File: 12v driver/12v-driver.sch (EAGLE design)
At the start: 42 parts, among them IC1 74AC14N, IC2 74AC14N, Q1 2N3906, Q2 2N3906, T1 2N3904, T2 2N3904, T3 2N3904, T4 2N3904, T5 2N3904, T6 2N3904

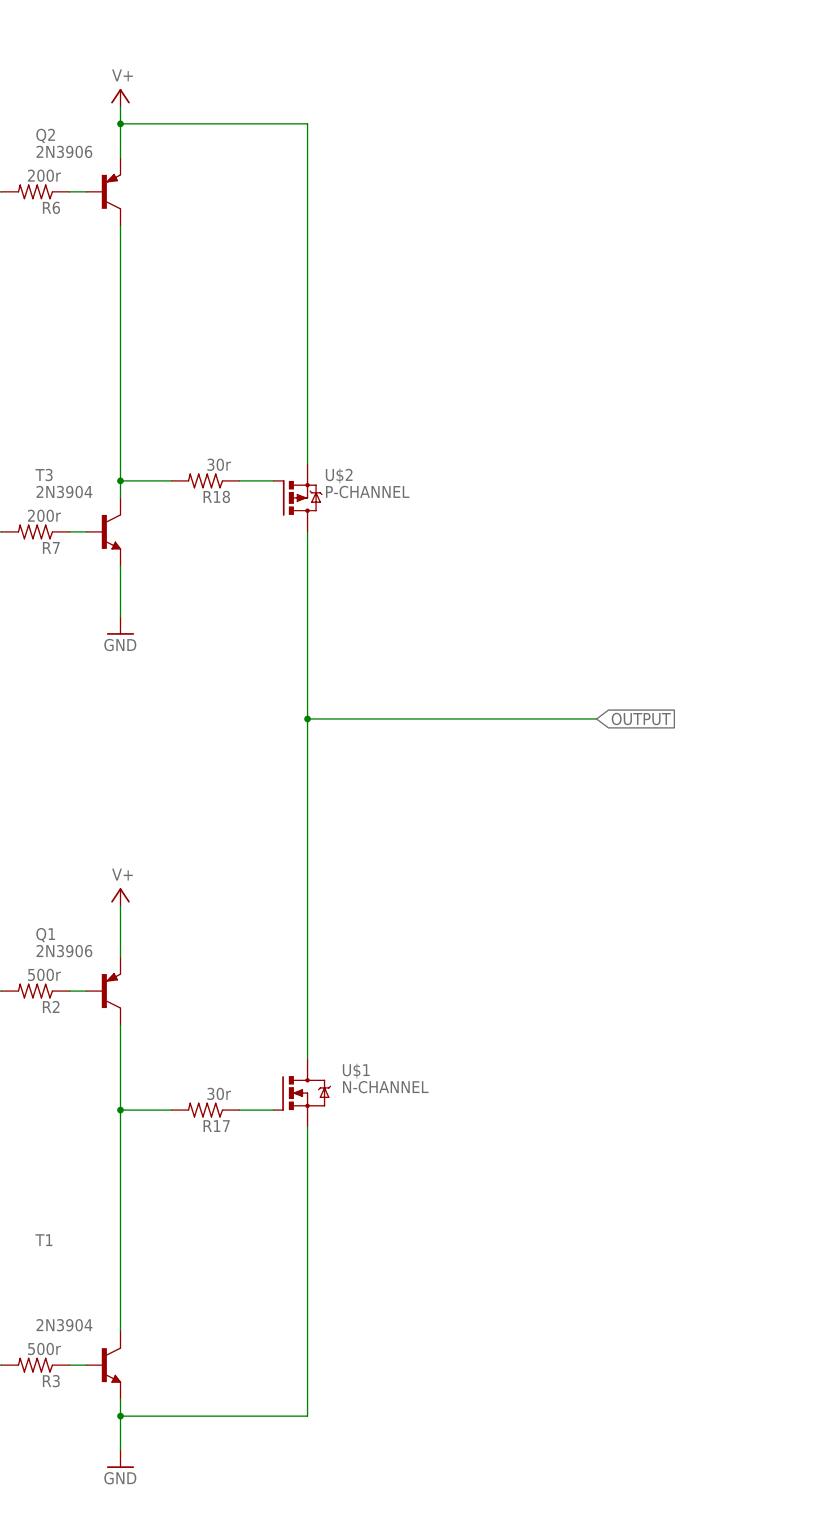
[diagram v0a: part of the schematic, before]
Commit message: added inverter to driver NPNs
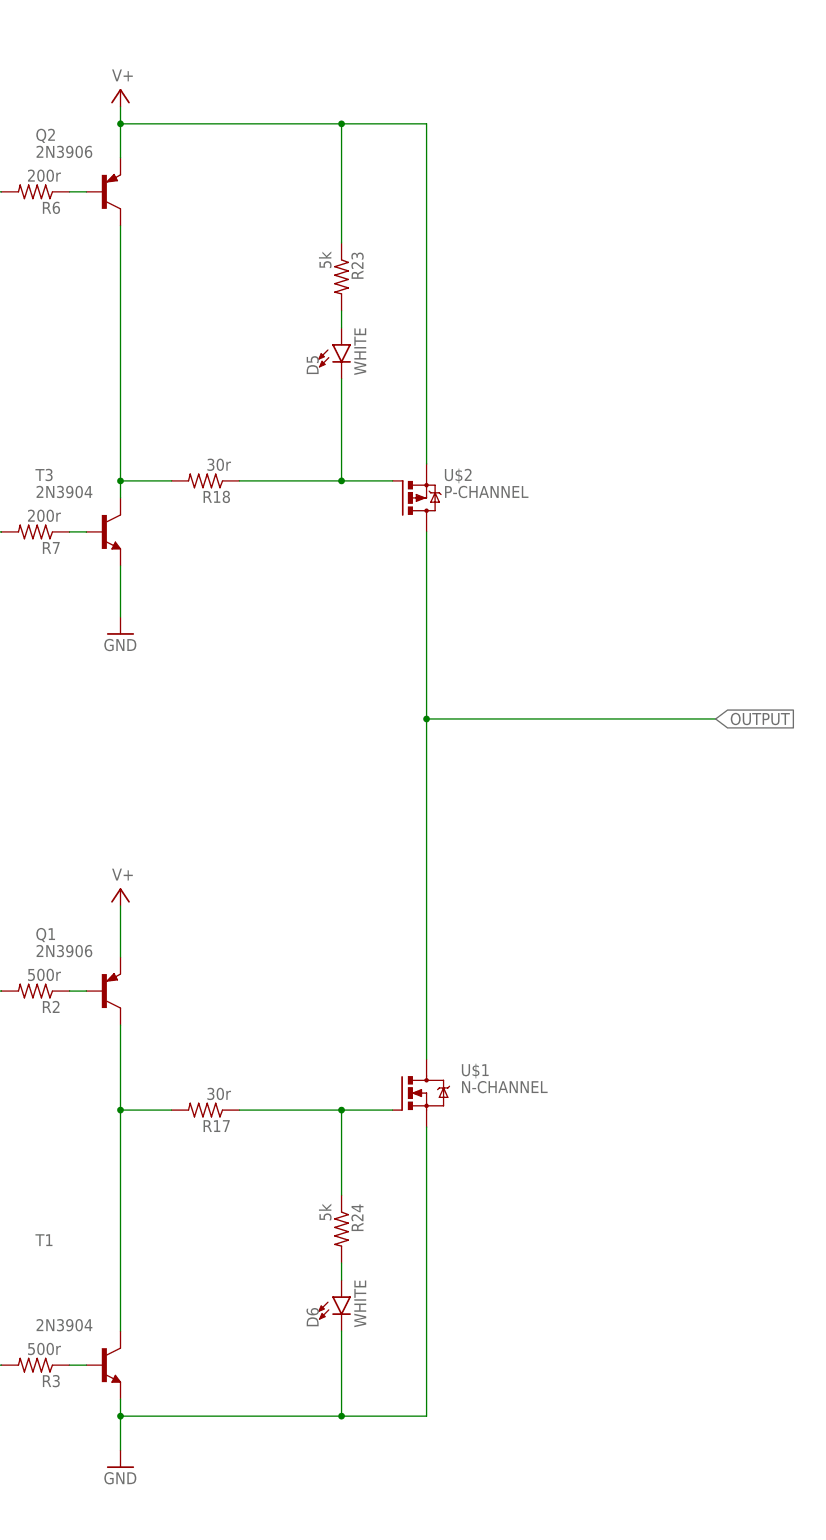
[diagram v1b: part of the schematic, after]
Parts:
- added D5, D6: WHITE, SparkFun-LED:LED-WHITE1206
- added R23, R24: 5k, rcl:R-US_R0603
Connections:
- new net N$29: D5.A, R23.2
- new net N$30: D6.A, R24.2
- net GND: now also D6.C
- net N$2: now also R24.1
- net N$8: now also D5.C
- net V+: now also R23.1
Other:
- moved on the sheet: U$1, U$2

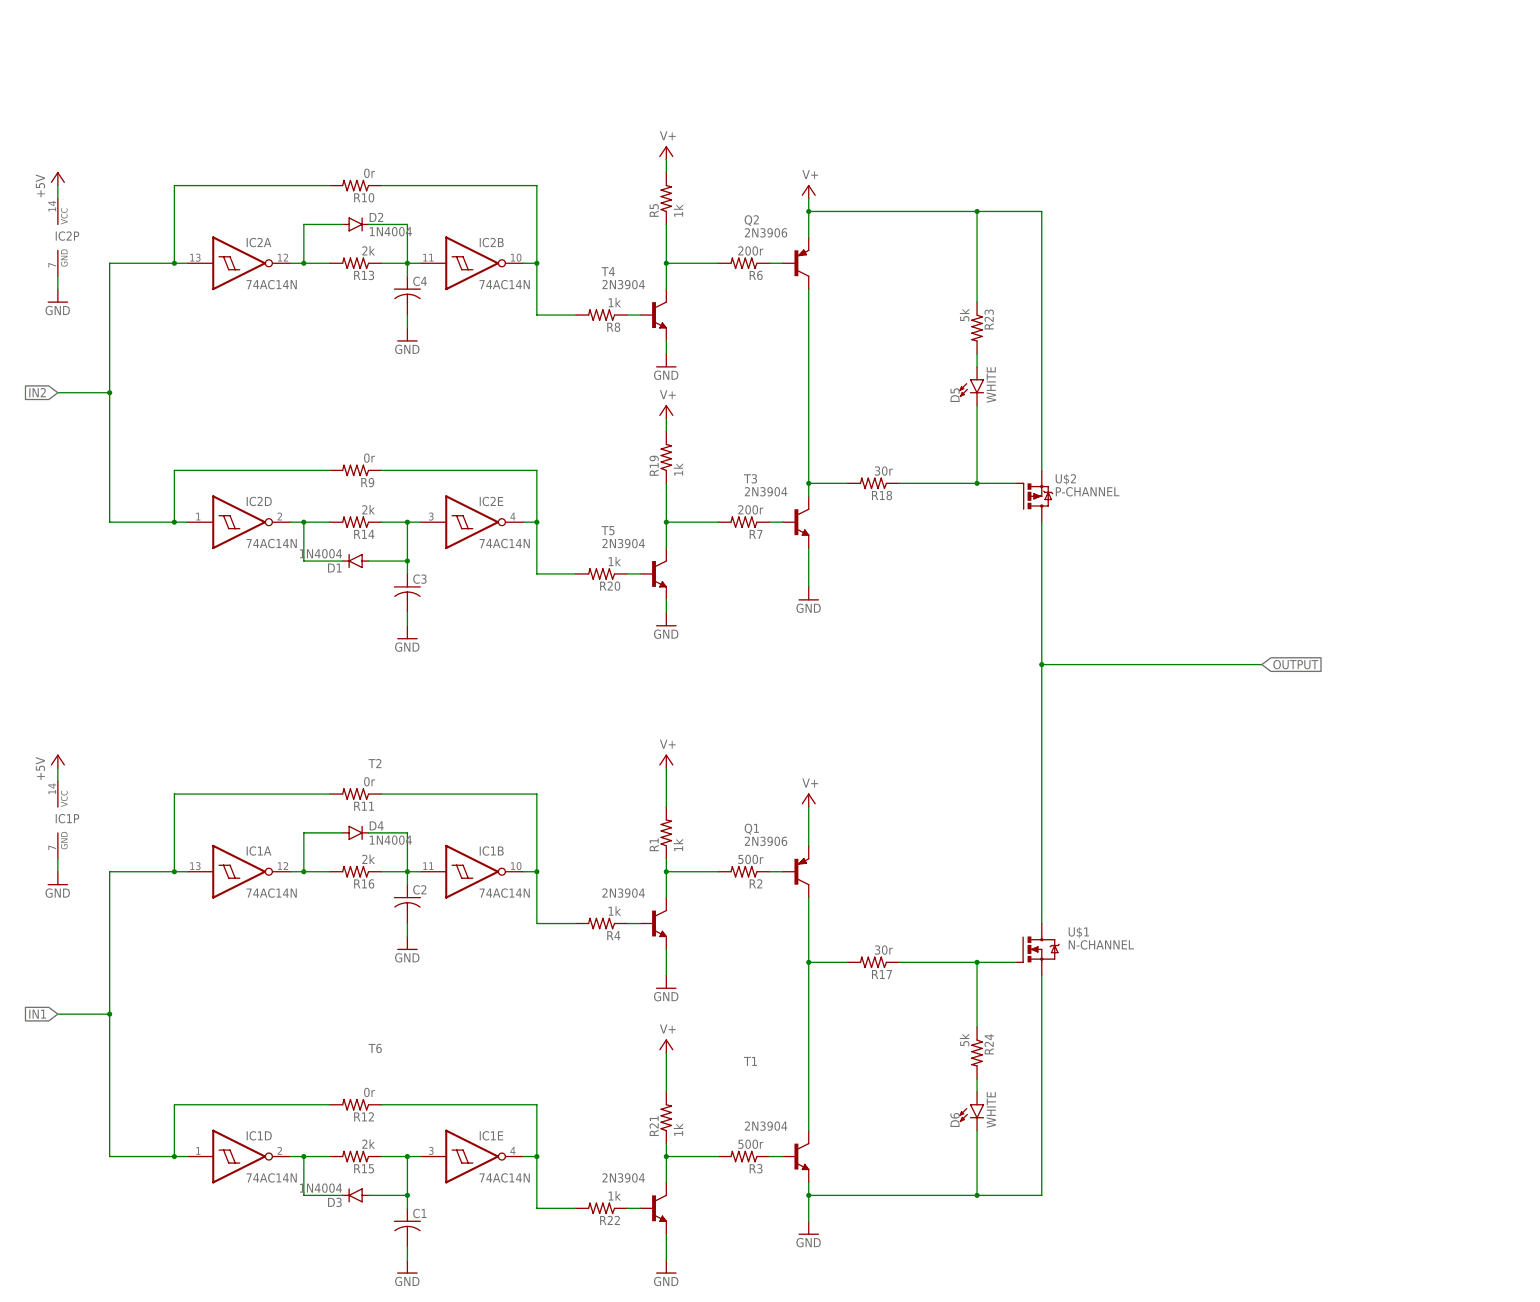
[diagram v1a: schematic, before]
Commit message: fixed production problems
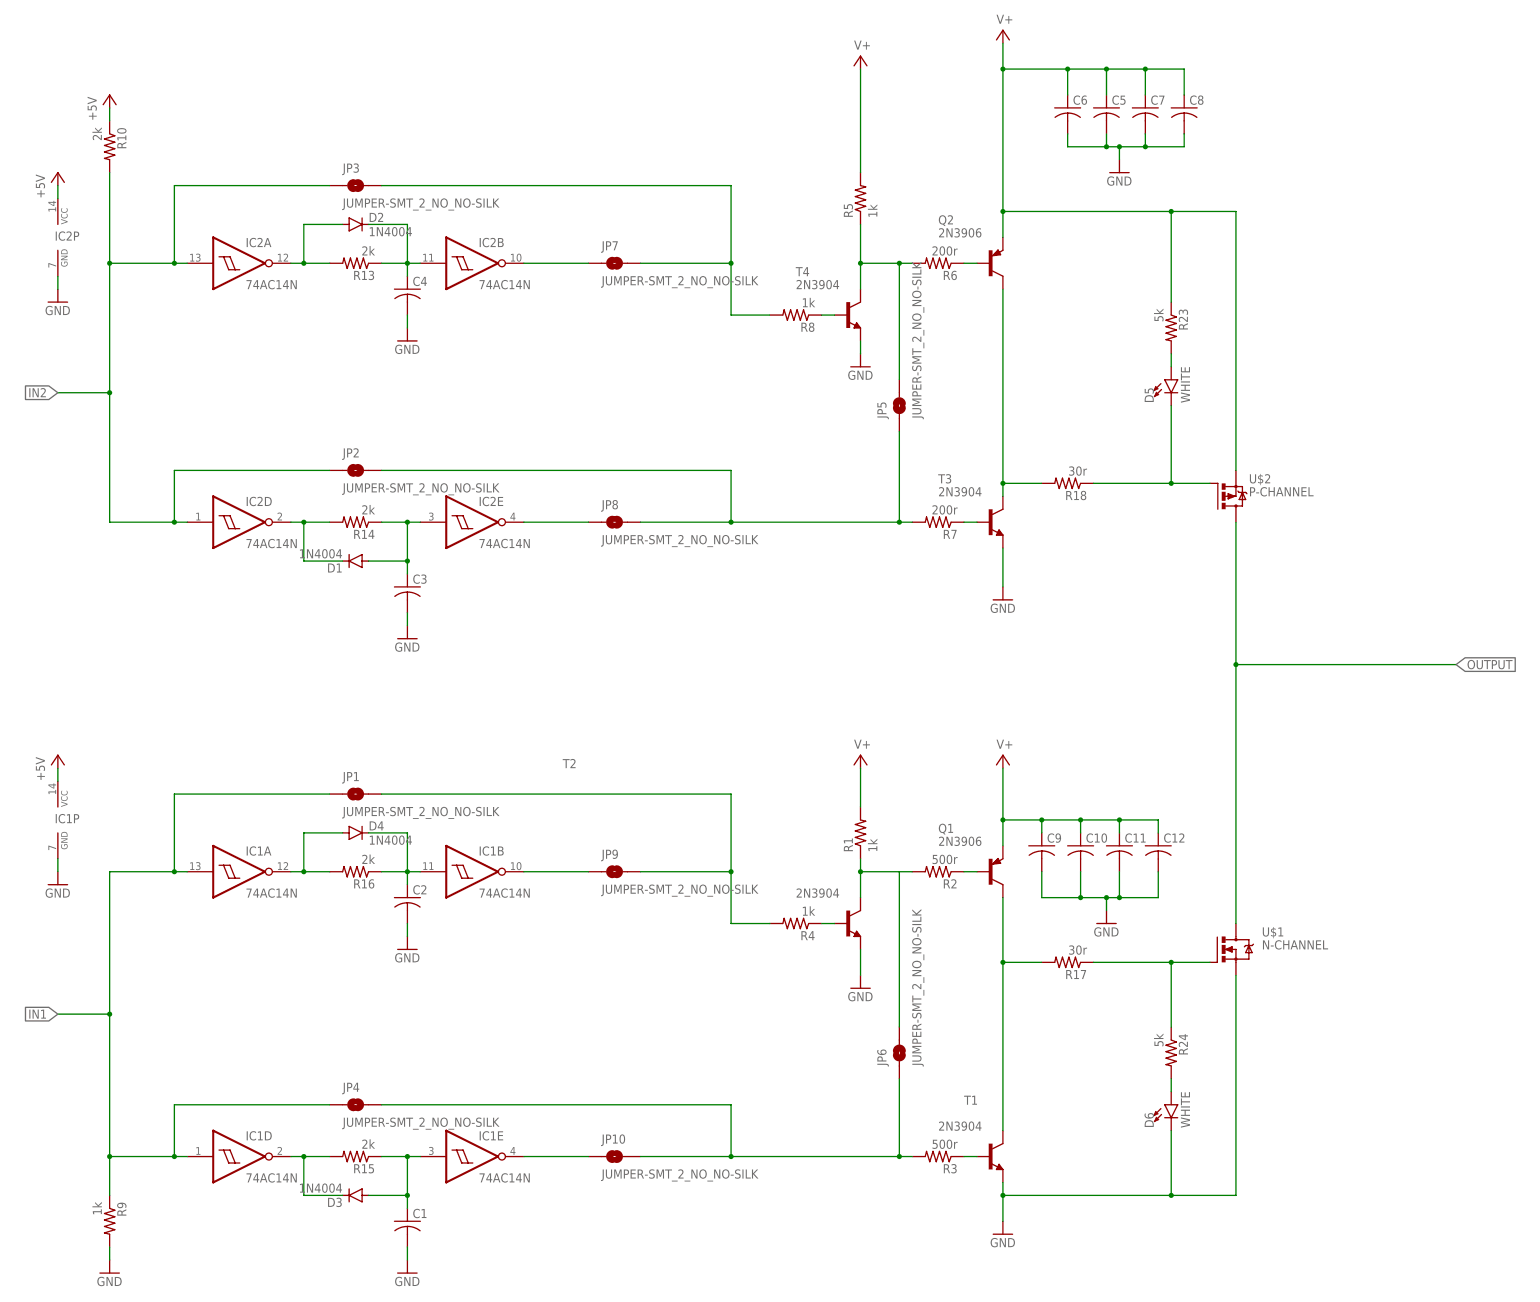
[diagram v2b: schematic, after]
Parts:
- removed R11, R12: 0r, rcl:R-US_R0603
- removed R19, R20, R21, R22: 1k, rcl:R-US_R0603
- removed T5, T6: 2N3904, transistor:2N3904
- added C10, C5: (no value), rcl:C-US050-024X044
- added C11, C12, C7, C8: (no value), rcl:C-USC0603
- added C6, C9: (no value), rcl:C-US075-032X103
- added JP1, JP10, JP2, JP3, JP4, JP5, JP6, JP7, JP8, JP9: JUMPER-SMT_2_NO_NO-SILK, SparkFun-Jumpers:JUMPER-SMT_2_NO_NO-SILK
- R10: value 0r -> 2k
- R9: value 0r -> 1k
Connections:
- net +5V: now also R10.1
- net GND: now also C10.2, C11.2, C12.2, C5.2, C6.2, C7.2, C8.2, C9.2, R9.2; no longer T5.E, T6.E
- net IN1: now also JP1.1, JP4.1, R9.1; no longer R11.2, R12.2
- net IN2: now also JP2.1, JP3.1; no longer R9.2
- net N$14: now also IC2B.O, JP7.1; no longer IC1E.O, R12.1, R22.2
- net N$15: now also JP2.2, JP5.1, JP8.2, R7.2; no longer R20.1, T5.B
- net N$17: now also JP1.2, JP9.2; no longer IC1B.O, R11.1
- net N$19: now also JP8.1; no longer R20.2, R9.1
- net N$21: now also JP3.2, JP7.2; no longer IC2B.O, R10.1
- net N$24: now also IC1B.O, JP9.1; no longer R22.1, T6.B
- net N$27: now also IC1E.O, JP10.1; no longer R19.1, R7.2, T5.C
- net N$28: now also JP10.2, JP4.2, JP6.1; no longer R21.1, T6.C
- net N$3: now also JP6.2
- net N$9: now also JP5.2
- net V+: now also C10.1, C11.1, C12.1, C5.1, C6.1, C7.1, C8.1, C9.1; no longer R19.2, R21.2
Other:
- moved on the sheet: D5, D6, Q1, Q2, R1, R10, R17, R18, R2, R23, R24, R3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

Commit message: started rework of new schematic
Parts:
- removed IC2: 74AC14N, 74xx-eu:74AC14N
- removed JP5, JP6: JUMPER-SMT_2_NO_NO-SILK, SparkFun-Jumpers:JUMPER-SMT_2_NO_NO-SILK
- removed T2, T3, T4: 2N3904, transistor:2N3904
- added C13, C14, C15, C16: (no value), rcl:C-USC0603
- added D10, D11, D12, D7, D8, D9: (no value), diode:DIODE-DO-214AC
- added IC3: 4081N, 40xx:4081N
- added IC4: 74AC14D, 74xx-eu:74AC14D
- added Q10, Q9: (no value), adafruit:MOSFET-NREFLOW
- added Q11, Q12: BSS84, Transistor:BSS84
- added Q13: 2N2907, adafruit:2N2907
- added Q3, Q4, Q5, Q6, Q7, Q8: BC618, transistor-npn:BC618
- added R11, R12, R19, R20: 1k, rcl:R-US_R0603
- added R21, R22, R25: 30r, rcl:R-US_R0603
- added U$3: STM32F070F6P6TR, Capstone:STM32F070F6P6TR
- D1, D2, D3, D4: value 1N4004 -> (none); device diode:1N4004 -> diode:DIODE-DO-214AC
- IC1: value 74AC14N -> 74AC14D; device 74xx-eu:74AC14N -> 74xx-eu:74AC14D
- Q1, Q2: value 2N3906 -> BC618; device transistor-pnp:2N3906 -> transistor-npn:BC618
- R17: value 30r -> 2k
- R2, R3: value 500r -> 300r
- R23, R24: value 5k -> 10k
- T1: value 2N3904 -> 2N2222; device transistor:2N3904 -> adafruit:2N2222
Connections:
- removed net +5V: IC1P.VCC, IC2P.VCC, R10.1
- new net +3V3: IC1P.VCC, IC4P.VCC, R10.1, U$3.VDD, U$3.VDDA
- new net ADC1: U$3.PA0
- new net ADC2: U$3.PA1
- new net ADC3: U$3.PA2
- new net ENABLE1: U$3.PA10
- new net ENABLE2: U$3.PA9
- new net ENABLE3: U$3.PA5
- new net HALF_VCC: U$3.PA3
- new net IN: Q13.B, T1.B
- new net N$31: C16.2, Q8.B, R12.1
- new net N$32: D12.C, Q7.B, Q8.C, R11.1
- new net N$33: C14.2, Q4.B, R20.1
- new net N$34: C14.1, JP2.2, JP8.2, R20.2
- new net N$35: D10.C, Q3.B, Q4.C, R19.1
- new net N$36: IC1A.I, IC3A.I1
- new net N$37: IC3A.I0, IC3B.I1
- new net N$38: IC3A.O, IC4A.I
- new net N$39: U$3.NRST
- new net N$40: Q12.D, R21.1
- new net N$41: D5.C, Q10.D, R22.2
- new net N$42: Q9.D, R25.2
- new net N$43: D9.A, Q1.E, R6.2
- new net N$44: D10.A, Q3.E, R7.2
- new net N$47: D11.A, Q5.E, R2.2
- new net N$48: D12.A, Q7.E, R3.2
- new net OUT: Q13.E, T1.E
- new net PWM1: U$3.PB1
- new net PWM2: U$3.PA7
- new net PWM3: U$3.PA6
- new net SWCLK: U$3.PA14
- new net SWDIO: U$3.PA13
- net GND: now also D8.A, IC4P.GND, Q10.S, Q13.C, Q2.E, Q4.E, Q6.E, Q8.E, Q9.S, R17.1, U$3.VSS; no longer IC2P.GND, T1.E, T2.E, T3.E, T4.E
- net IN1: now also IC1B.I, IC1E.I, IC3B.O; no longer IC1A.I, IC1D.I
- net IN2: now also IC4A.O, IC4B.I, IC4E.I; no longer IC2A.I, IC2D.I
- net N$1: now also R18.2, R25.1, U$1.G; no longer Q1.C, R17.2, T1.C
- net N$10: now also Q12.G; no longer Q2.B
- net N$11: now also Q10.G; no longer T3.B
- net N$12: now also C13.2, Q2.B; no longer T4.B
- net N$13: now also IC1B.O; no longer IC1A.O
- net N$14: now also IC4C.O; no longer IC2B.O
- net N$15: now also IC1A.O, IC3B.I0; no longer JP2.2, JP5.1, JP8.2, R7.2
- net N$16: now also IC1C.I; no longer IC1B.I
- net N$17: now also C15.1
- net N$18: now also IC4F.I; no longer IC2E.I
- net N$19: now also IC4F.O; no longer IC2E.O
- net N$2: now also R17.2, U$3.BOOT0; no longer R17.1, R24.1, U$1.G
- net N$20: now also IC4C.I; no longer IC2B.I
- net N$21: now also C13.1
- net N$22: now also IC4B.O; no longer IC2A.O
- net N$23: now also IC4E.O; no longer IC2D.O
- net N$24: now also IC1C.O; no longer IC1B.O
- net N$25: now also IC1E.O; no longer IC1D.O
- net N$26: now also IC1F.I; no longer IC1E.I
- net N$27: now also IC1F.O; no longer IC1E.O
- net N$28: now also C16.1, R12.2; no longer JP6.1, R3.2
- net N$3: now also D11.C, Q5.B, Q6.C; no longer JP6.2, R2.2, T2.C
- net N$4: now also Q11.G; no longer Q1.B
- net N$5: no longer T1.B
- net N$6: now also C15.2, Q6.B; no longer T2.B
- net N$7: now also R21.2, R22.1, U$2.G; no longer Q2.C, R18.2, T3.C
- net N$8: now also Q11.D, R24.1; no longer D5.C, U$2.G
- net N$9: now also D9.C, Q1.B, Q2.C; no longer JP5.2, R6.2, T4.C
- net OUTPUT: now also D7.A, D8.C
- net V+: now also D7.C, Q1.C, Q11.S, Q12.S, Q3.C, Q5.C, Q7.C, R11.2, R19.2, T1.C; no longer Q1.E, Q2.E
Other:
- moved on the sheet: C10, C11, C12, C4, C5, C6, C7, C8, C9, D5, D6, IC1A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

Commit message: started routing v2
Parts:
- removed D1, D2, D3, D4: (no value), diode:DIODE-DO-214AC
- removed IC3: 4081N, 40xx:4081N
- removed Q10, Q9: (no value), adafruit:MOSFET-NREFLOW
- removed Q11, Q12: BSS84, Transistor:BSS84
- removed Q13: 2N2907, adafruit:2N2907
- removed T1: 2N2222, adafruit:2N2222
- added JP11, JP12, JP5, JP6: JUMPER-SMT_2_NO_NO-SILK, SparkFun-Jumpers:JUMPER-SMT_2_NO_NO-SILK
- added R26, R27: 10k, rcl:R-US_R0603
- added U$10, U$11, U$12, U$9: DSS110UTR, BLDC:DSS110UTR
- added U$4: TC7PZ14FU,LJ(CT, BLDC:TC7PZ14FU,LJ(CT
- added U$5, U$6: SI2372DS-T1-GE3, BLDC:SI2372DS-T1-GE3
- added U$7, U$8: DMP2100U-7, BLDC:DMP2100U-7
- added U1: SN74LVC2G08DCURDCU8-M, BLDC:SN74LVC2G08DCURDCU8-M
- Q1, Q2, Q3, Q4, Q5, Q6, Q7, Q8: value BC618 -> 2N3904; device transistor-npn:BC618 -> BLDC:2N3904
- R10: value 2k -> 1k
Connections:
- removed net IN: Q13.B, T1.B
- removed net N$36: IC1A.I, IC3A.I1
- removed net N$37: IC3A.I0, IC3B.I1
- removed net OUT: Q13.E, T1.E
- new net DIRECTION: R9.1, U$4G$2.I, U1G$1.I1
- new net ENABLE: R10.1, U1G$1.I0, U1G$2.I1
- net +3V3: now also U$4G$3.VCC, U1G$3.VCC; no longer R10.1
- net GND: now also Q1.E, Q3.E, Q7.E, R10.2, R27.2, U$4G$3.GND, U$5.S, U$6.S, U1G$3.GND; no longer Q10.S, Q13.C, Q4.E, Q6.E, Q8.E, Q9.S
- net IN1: now also U1G$2.O; no longer IC3B.O, R9.1
- net IN2: now also U$4G$1.O; no longer IC4A.O, R10.2
- net N$1: now also R27.1
- net N$10: now also JP5.2, U$7.G; no longer Q12.G
- net N$11: now also JP5.1, U$6.G; no longer Q10.G
- net N$12: now also Q1.B; no longer Q2.B
- net N$13: now also U$10.A; no longer D4.A
- net N$15: now also U$4G$2.O, U1G$2.I0; no longer IC1A.O, IC3B.I0
- net N$16: now also U$10.C; no longer D4.C
- net N$18: now also U$12.A; no longer D1.A
- net N$20: now also U$11.C; no longer D2.C
- net N$22: now also U$11.A; no longer D2.A
- net N$23: now also U$12.C; no longer D1.C
- net N$25: now also U$9.C; no longer D3.C
- net N$26: now also U$9.A; no longer D3.A
- net N$3: now also Q3.C, Q4.B; no longer Q5.B, Q6.C
- net N$31: now also Q7.B; no longer Q8.B
- net N$32: now also Q7.C, Q8.B; no longer Q7.B, Q8.C
- net N$33: now also Q2.B; no longer Q4.B
- net N$35: now also Q2.C, Q5.B; no longer Q3.B, Q4.C
- net N$38: now also U$4G$1.I, U1G$1.O; no longer IC3A.O, IC4A.I
- net N$4: now also JP12.2, U$8.G; no longer Q11.G
- net N$40: now also U$7.D; no longer Q12.D
- net N$41: now also U$6.D; no longer Q10.D
- net N$42: now also U$5.D; no longer Q9.D
- net N$43: now also JP6.2, Q6.E; no longer Q1.E
- net N$44: now also JP6.1, Q5.E; no longer Q3.E
- net N$47: now also JP11.2, Q4.E; no longer Q5.E
- net N$48: now also JP11.1, Q8.E; no longer Q7.E
- net N$5: now also JP12.1, U$5.G
- net N$6: now also Q3.B; no longer Q6.B
- net N$7: now also R26.2
- net N$8: now also U$8.D; no longer Q11.D
- net N$9: now also Q1.C, Q6.B; no longer Q1.B, Q2.C
- net V+: now also Q4.C, Q6.C, Q8.C, R26.1, U$7.S, U$8.S; no longer Q1.C, Q11.S, Q12.S, Q3.C, Q7.C, T1.C
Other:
- moved on the sheet: D6, IC1P, IC4P, Q1, Q2, Q3, Q4, Q5, Q6, Q7, Q8, R10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
